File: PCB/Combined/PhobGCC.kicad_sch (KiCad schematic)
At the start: 72 parts, among them J1 Conn_01x06_Female, J2 Conn_01x04_Female, J3 Conn_01x01_Male, J4 Conn_01x04_Male, J5 Conn_01x02_Male, Q1 Q_NMOS_GSD, Q2 Q_PMOS_GDS, Q3 Q_NMOS_GSD, SW1 A, SW10 Dup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

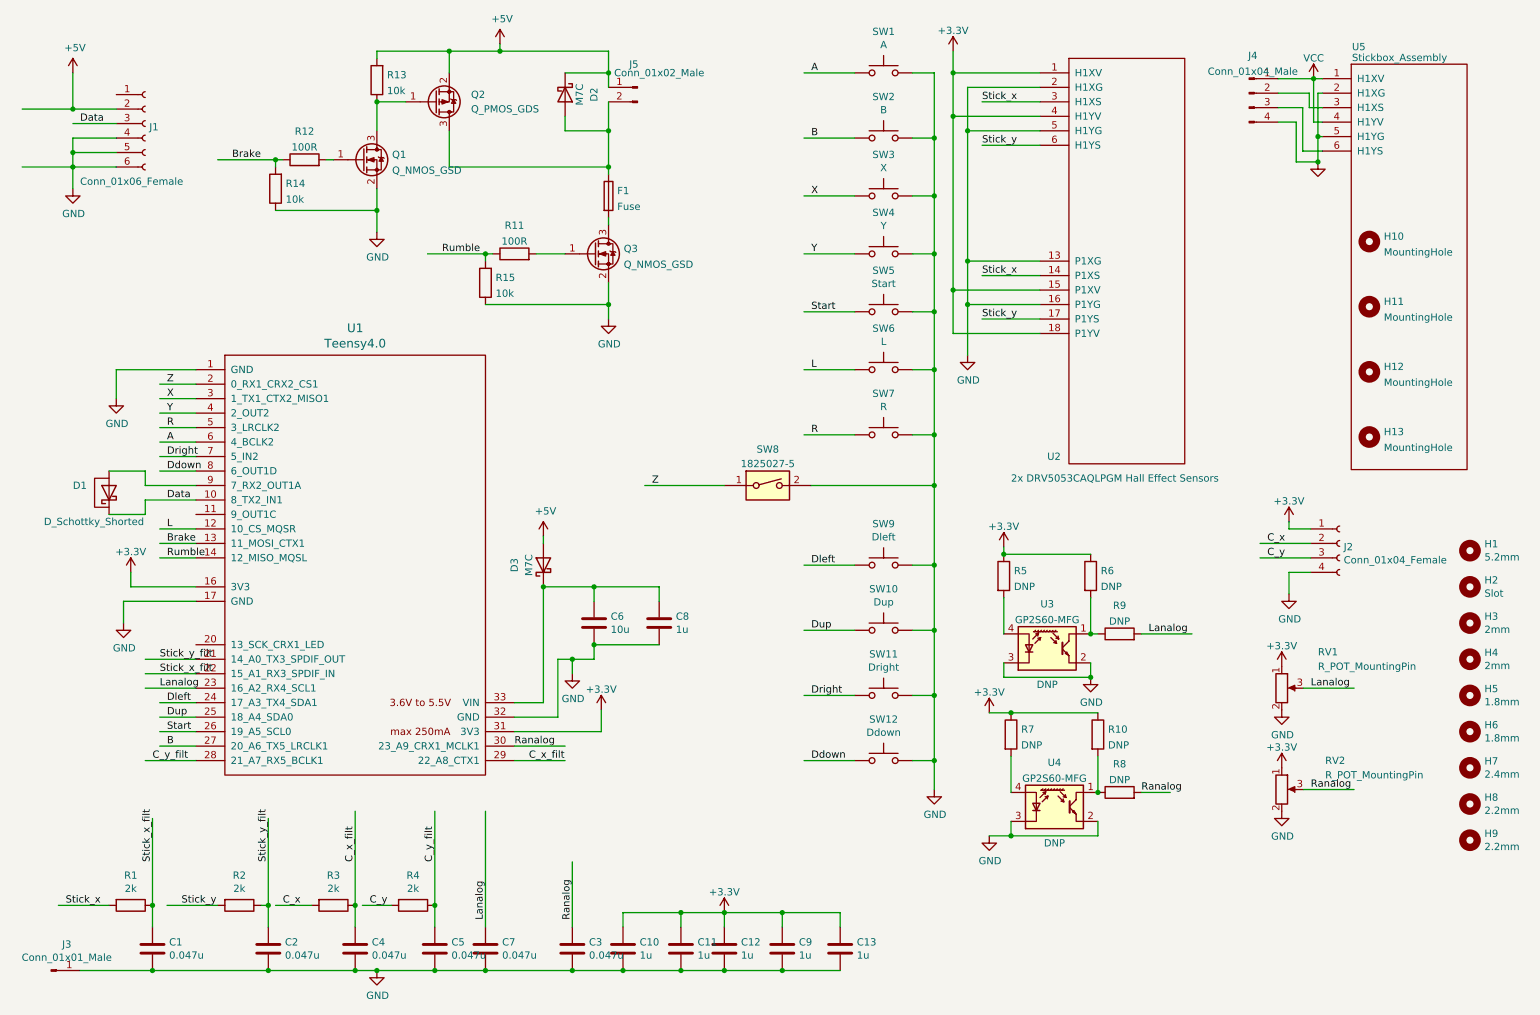
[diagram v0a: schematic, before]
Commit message: rebuild for 1.2.1
added JST connector for rumble, button pinout, fixed outline, removed unused trigger sensors.
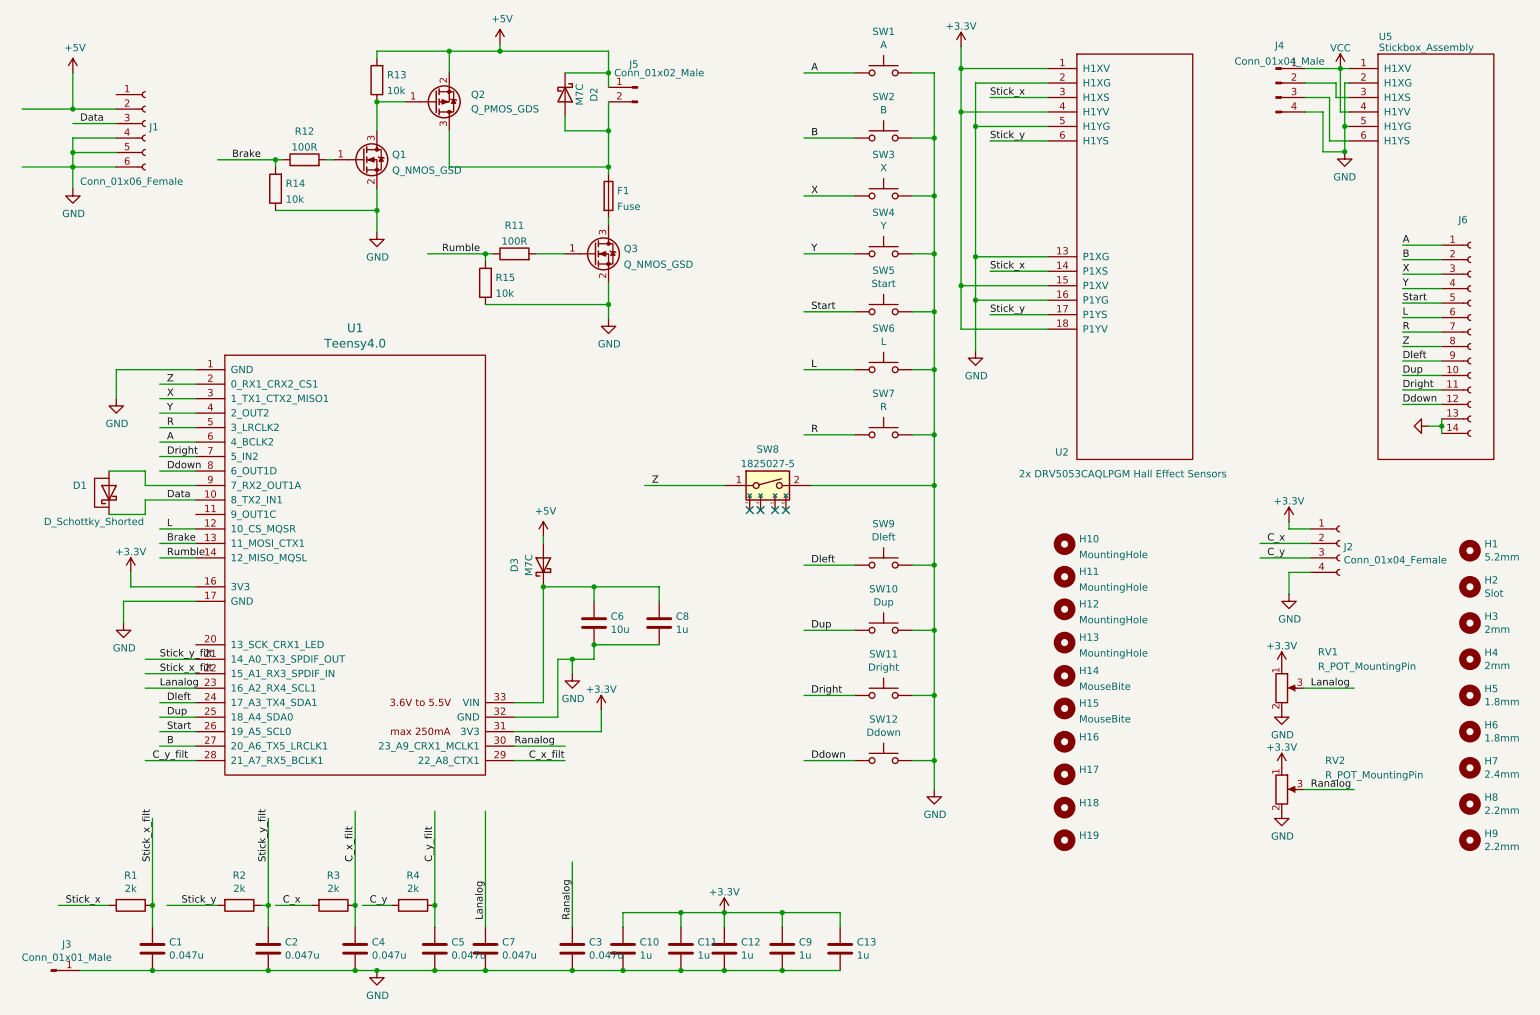
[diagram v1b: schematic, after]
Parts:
- removed R10, R5, R6, R7, R8, R9: DNP, Resistor_SMD:R_0603_1608Metric_Pad0.98x0.95mm_HandSolder, symbol Device:R
- removed U3, U4: GP2S60-MFG, PhobGCC_Footprints:Sharp_Microelectronics-GP2S60-MFG, symbol Sensor_Proximity:BPR-105
- added H14, H15: MouseBite, symbol Mechanical:MountingHole
- added H16, H17, H18, H19: (no value), symbol Mechanical:MountingHole
- added J6: (no value), symbol Connector:Conn_01x14_Female
- C1, C2, C3, C4, C5, C6, C7: footprint Capacitors_SMD:C_0603_HandSoldering -> (none)
- C10, C11, C12, C13, C8, C9: footprint Capacitor_SMD:C_0603_1608Metric_Pad1.08x0.95mm_HandSolder -> (none)
- D1: footprint Gamecube MB:D_SOD-523_Shorted -> (none)
- D2, D3: footprint Diode_SMD:D_SOD-123 -> (none)
- F1: footprint Resistor_SMD:R_1206_3216Metric -> (none)
- H1: footprint PhobGCC_Footprints:MountingHole_5.2mm -> (none)
- H2: footprint PhobGCC_Footprints:Slot -> (none)
- H3, H4: footprint PhobGCC_Footprints:MountingHole_2.0mm -> (none)
- H5, H6: footprint PhobGCC_Footprints:MountingHole_1.8mm -> (none)
- H7: footprint PhobGCC_Footprints:MountingHole_2.4mm -> (none)
- H8, H9: footprint PhobGCC_Footprints:MountingHole_2.2mm -> (none)
- J1: footprint PhobGCC_Footprints:GCC_Header_Straight_1x06_Pitch2.00mm -> (none)
- J2: footprint Pin_Headers:Pin_Header_Straight_1x04_Pitch2.00mm -> (none)
- J3: footprint Connector_PinHeader_2.54mm:PinHeader_1x01_P2.54mm_Vertical -> (none)
- J4: footprint Connector_PinHeader_2.00mm:PinHeader_1x04_P2.00mm_Vertical -> (none)
- J5: footprint Connector_PinHeader_2.54mm:PinHeader_1x02_P2.54mm_Vertical -> (none)
- Q1, Q2, Q3: footprint Package_TO_SOT_SMD:SOT-23 -> (none)
- R1, R11, R12, R13, R14, R15, R2, R3, R4: footprint Resistor_SMD:R_0603_1608Metric_Pad0.98x0.95mm_HandSolder -> (none)
- RV1, RV2: footprint PhobGCC_Footprints:GCC_Slider -> (none)
- SW1, SW2, SW3, SW4: footprint PhobGCC_Footprints:ABXY_Contact_Omron_Switch -> (none)
- SW10, SW11, SW12, SW9: footprint PhobGCC_Footprints:Dpad_Contact_TL3315NF_2 -> (none)
- SW5: footprint PhobGCC_Footprints:Start_Contact -> (none)
- SW6, SW7: footprint Pin_Headers:Pin_Header_Straight_1x02_Pitch2.54mm -> (none)
- SW8: footprint PhobGCC_Footprints:Z_Switch_Edge -> (none); symbol Switch:SW_DIP_x01 -> PhobGCC_Symbol_Library:SW_DIP_x01
- U1: footprint teensy:Teensy40_Edge_Pins -> (none)
- U2: footprint PhobGCC_Footprints:GCC_Stickbox_2 -> (none)
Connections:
- net A: now also J6.1 (Pin_1)
- net B: now also J6.2 (Pin_2)
- net Ddown: now also J6.12 (Pin_12)
- net Dleft: now also J6.9 (Pin_9)
- net Dright: now also J6.11 (Pin_11)
- net Dup: now also J6.10 (Pin_10)
- net GND: now also J6.13 (Pin_13), J6.14 (Pin_14)
- net L: now also J6.6 (Pin_6)
- net R: now also J6.7 (Pin_7)
- net Start: now also J6.5 (Pin_5)
- net X: now also J6.3 (Pin_3)
- net Y: now also J6.4 (Pin_4)
- net Z: now also J6.8 (Pin_8)
- no-connect marks 0 -> 4
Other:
- moved on the sheet: U2

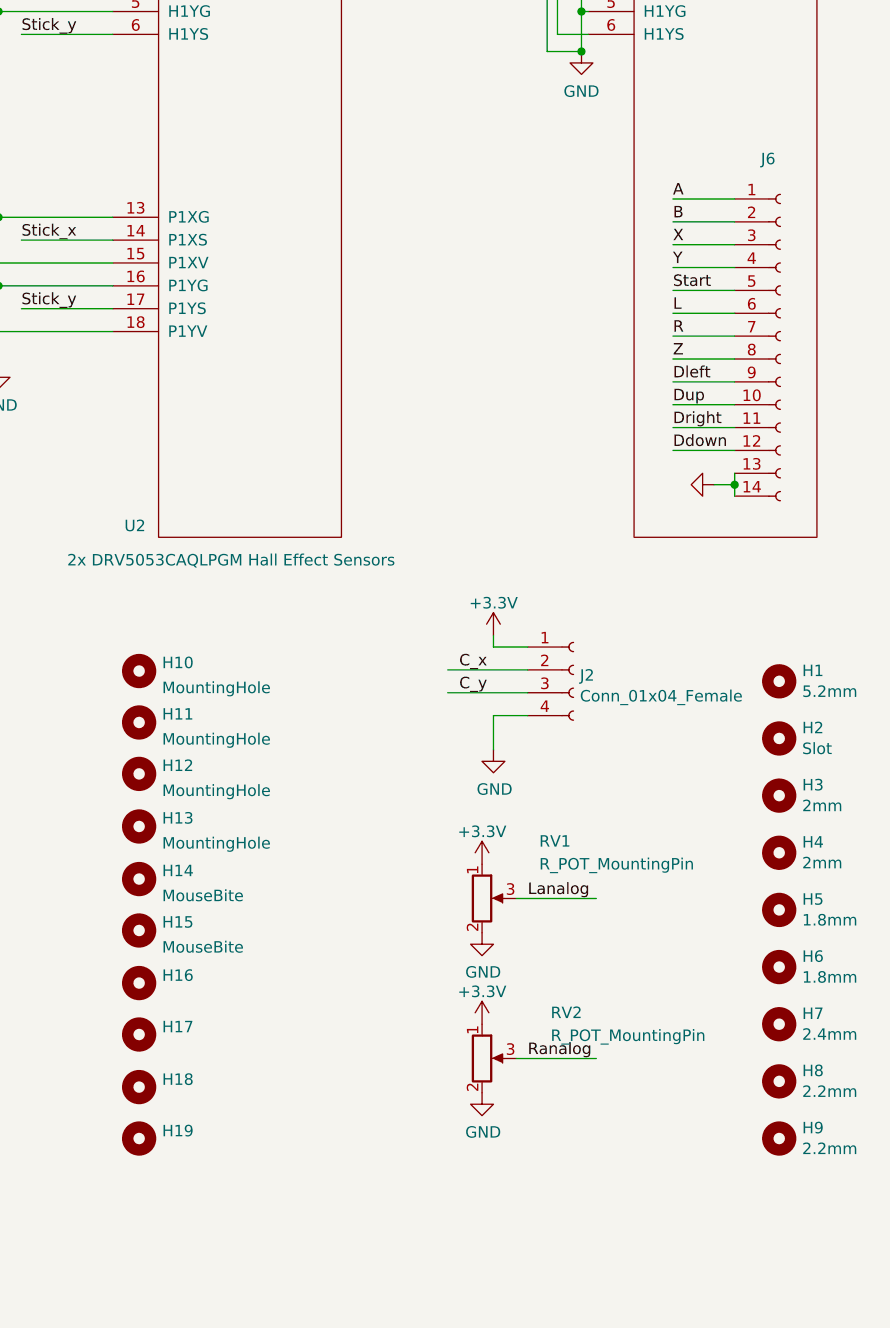
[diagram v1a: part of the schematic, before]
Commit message: hatched fill added
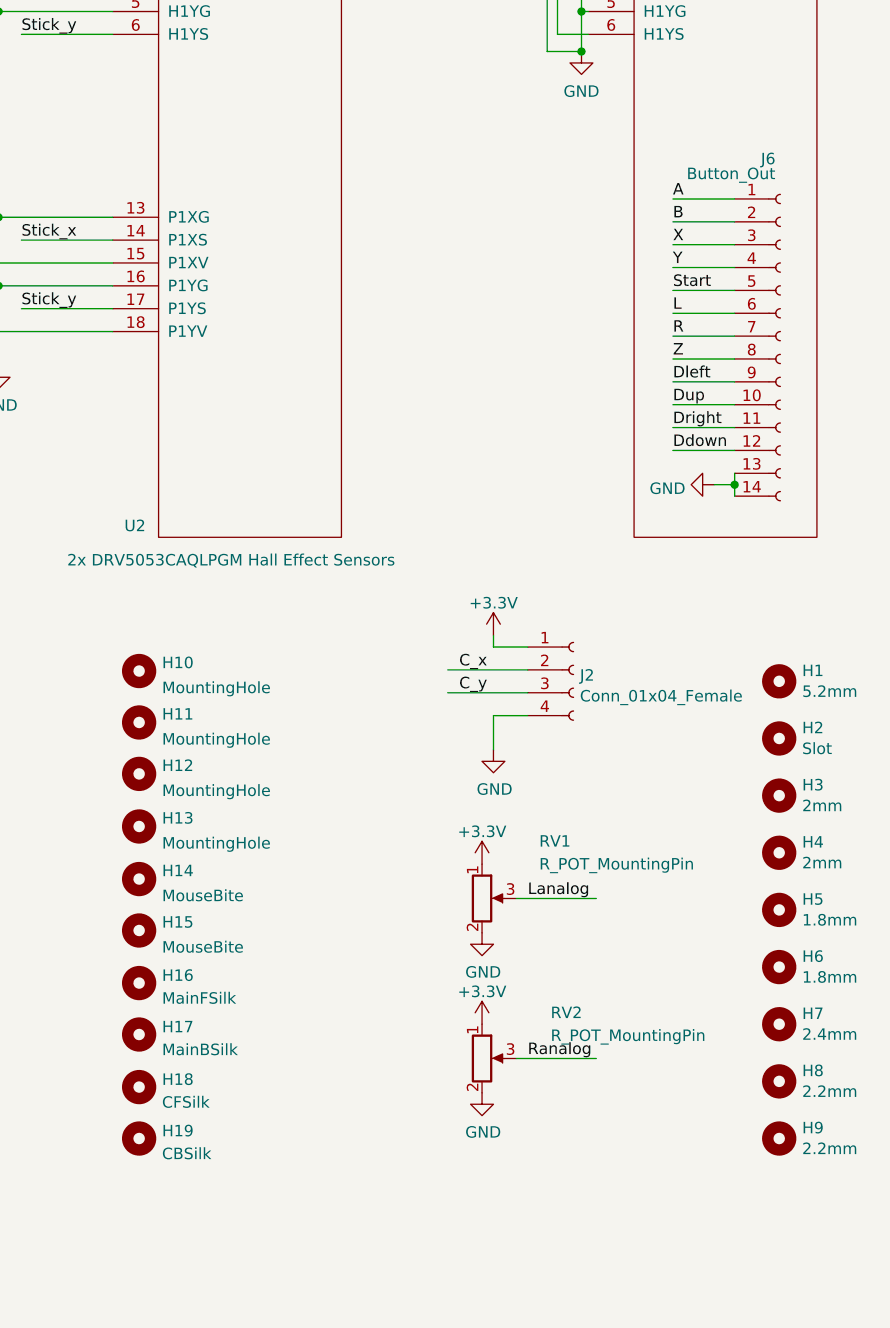
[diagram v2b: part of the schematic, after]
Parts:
- C1, C2, C3, C4, C5, C6, C7: footprint (none) -> wavbrd:C_0603_HandSoldering
- C10, C11, C12, C13, C8, C9: footprint (none) -> wavbrd:C_0603_1608Metric_Pad1.08x0.95mm_HandSolder
- D1: footprint (none) -> wavbrd:D_SOD-523_Shorted
- D2, D3: footprint (none) -> wavbrd:D_SOD-123
- F1: footprint (none) -> wavbrd:R_1206_3216Metric
- H1, H11: footprint (none) -> wavbrd:MountingHole_5.2mm
- H10, H5, H6: footprint (none) -> wavbrd:MountingHole_1.8mm
- H12, H13, H3, H4: footprint (none) -> wavbrd:MountingHole_2.0mm
- H14, H15: footprint (none) -> wavbrd:mouse-bite-2.54mm-slot
- H16: value (none) -> MainFSilk; footprint (none) -> wavbrd:wavbrd_silk
- H17: value (none) -> MainBSilk; footprint (none) -> wavbrd:wavbrd_backsilk
- H18: value (none) -> CFSilk; footprint (none) -> wavbrd:cstick_silk
- H19: value (none) -> CBSilk; footprint (none) -> wavbrd:cstick_backsilk
- H2: footprint (none) -> wavbrd:Slot
- H7: footprint (none) -> wavbrd:MountingHole_2.4mm
- H8, H9: footprint (none) -> wavbrd:MountingHole_2.2mm
- J1: footprint (none) -> wavbrd:GCC_Header_Straight_1x06_Pitch2.00mm
- J2: footprint (none) -> wavbrd:Pin_Header_Straight_1x04_Pitch2.00mm
- J3: footprint (none) -> wavbrd:PinHeader_1x01_P2.54mm_Vertical
- J4: footprint (none) -> wavbrd:PinHeader_1x04_P2.00mm_Vertical
- J6: value (none) -> Button_Out; footprint (none) -> wavbrd:PinSocket_2x07_P2.54mm_Vertical
- Q1, Q2, Q3: footprint (none) -> wavbrd:SOT-23
- R1, R11, R12, R13, R14, R15, R2, R3, R4: footprint (none) -> wavbrd:R_0603_1608Metric_Pad0.98x0.95mm_HandSolder
- RV1, RV2: footprint (none) -> wavbrd:GCC_Slider
- SW1, SW2, SW3, SW4: footprint (none) -> wavbrd:ABXY_Contact_Omron_Switch
- SW10, SW11, SW12, SW9: footprint (none) -> wavbrd:Dpad_Contact_TL3315NF_2
- SW5: footprint (none) -> wavbrd:Start_Contact
- SW6, SW7: footprint (none) -> wavbrd:Pin_Header_Straight_1x02_Pitch2.54mm
- SW8: footprint (none) -> wavbrd:Z_Switch_Edge
- U1: footprint (none) -> wavbrd:Teensy40_Edge_Pins
- U2: footprint (none) -> wavbrd:GCC_Stickbox_2
- U5: footprint (none) -> wavbrd:GCC_Stickbox_Hall_Only
